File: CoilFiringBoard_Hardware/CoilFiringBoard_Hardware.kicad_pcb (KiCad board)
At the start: 2 copper layers, 101.6 x 76.2 mm, 22 parts, among them Q1 Q_NMOS_GDS, Q2 Q_NMOS_GDS

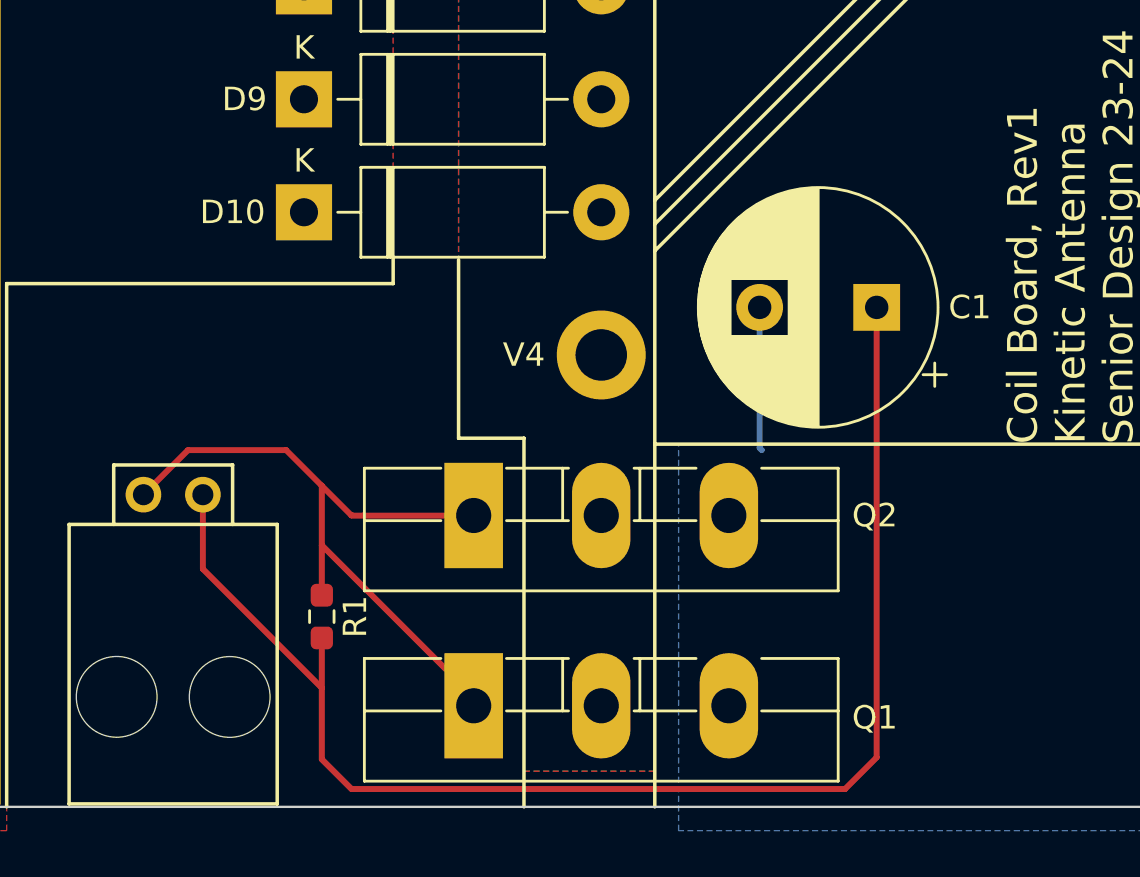
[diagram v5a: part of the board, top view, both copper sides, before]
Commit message: Adjusted gate traces
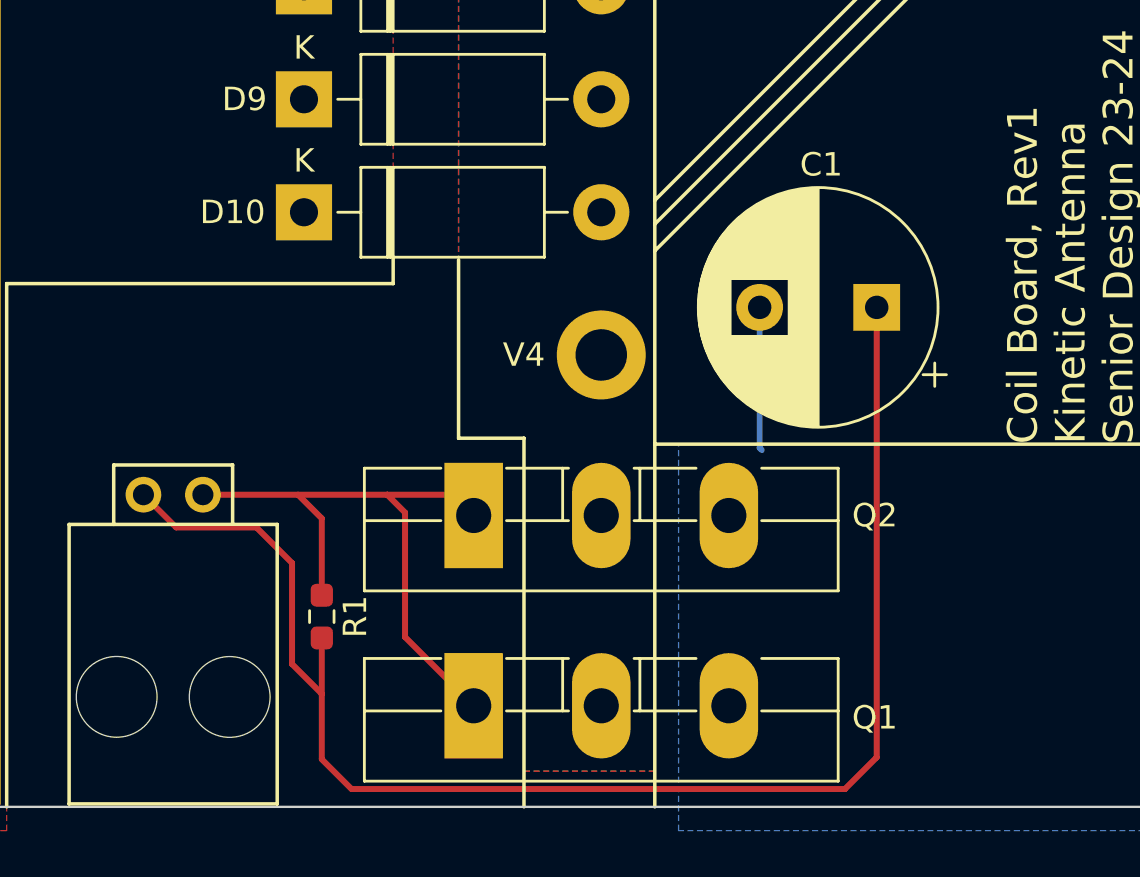
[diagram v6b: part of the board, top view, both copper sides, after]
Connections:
- Conn1 pad 1: GND1 -> Net-(Q1-G)
- Conn1 pad 2: Net-(Q1-G) -> GND1
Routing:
- net GND1: track 59.6 -> 62.9 mm
- net Net-(Q1-G): track 30.3 -> 27.2 mm
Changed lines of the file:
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@@
     (property "ki_keywords" "cap capacitor")
     (attr through_hole)
-    (fp_text reference "C1" (at -3.982323 0) (layer "F.SilkS")
+    (fp_text reference "C1" (at 2.367677 6.096) (layer "F.SilkS")
         (effects (font (size 1 1) (thickness 0.15)))
     )
@@
     (pad "" np_thru_hole circle (at 3.683 -8.636 180) (size 3.45 3.45) (drill 3.45) (layers "*.Cu" "*.Mask"))
     (pad "1" thru_hole circle (at 0 0 180) (size 1.524 1.524) (drill 0.9) (layers "*.Cu" "*.Mask")
+      (net 2 "Net-(Q1-G)") (pintype "input"))
+    (pad "2" thru_hole circle (at 2.54 0 180) (size 1.524 1.524) (drill 0.9) (layers "*.Cu" "*.Mask")
       (net 1 "GND1") (pintype "input"))
-    (pad "2" thru_hole circle (at 2.54 0 180) (size 1.524 1.524) (drill 0.9) (layers "*.Cu" "*.Mask")
-      (net 2 "Net-(Q1-G)") (pintype "input"))
     (model "${MRDT_KICAD_LIBRARIES}/3D Files/MRDT_Connctors/Molex_SL_02_Horizontal.stp"
       (offset (xyz 5.079999924 12.95399981 0))
@@
     (style (thickness 0.15) (arrow_length 1.27) (text_position_mode 0) (extension_height 0.58642) (extension_offset 0.5) keep_text_aligned)
   )
-  (segment (start 97.536 101.473) (end 97.536 104.648) (width 0.254) (layer "F.Cu") (net 1))
-  (segment (start 102.616 109.728) (end 102.616 112.776) (width 0.254) (layer "F.Cu") (net 1))
+  (segment (start 101.346 104.394) (end 99.822 102.87) (width 0.254) (layer "F.Cu") (net 1))
   (segment (start 103.886 114.046) (end 124.968 114.046) (width 0.254) (layer "F.Cu") (net 1))
+  (segment (start 102.616 109.982) (end 101.346 108.712) (width 0.254) (layer "F.Cu") (net 1))
   (segment (start 126.319677 112.694323) (end 126.319677 93.472) (width 0.254) (layer "F.Cu") (net 1))
-  (segment (start 97.536 104.648) (end 102.616 109.728) (width 0.254) (layer "F.Cu") (net 1))
+  (segment (start 102.616 107.5925) (end 102.616 109.982) (width 0.254) (layer "F.Cu") (net 1))
+  (segment (start 102.616 112.776) (end 103.886 114.046) (width 0.254) (layer "F.Cu") (net 1))
+  (segment (start 101.346 108.712) (end 101.346 104.394) (width 0.254) (layer "F.Cu") (net 1))
   (segment (start 124.968 114.046) (end 126.319677 112.694323) (width 0.254) (layer "F.Cu") (net 1))
-  (segment (start 102.616 107.5925) (end 102.616 109.728) (width 0.254) (layer "F.Cu") (net 1))
-  (segment (start 102.616 112.776) (end 103.886 114.046) (width 0.254) (layer "F.Cu") (net 1))
-  (segment (start 109.104 110.49) (end 109.104 110.12) (width 0.254) (layer "F.Cu") (net 2))
-  (segment (start 96.901 99.568) (end 94.996 101.473) (width 0.254) (layer "F.Cu") (net 2))
-  (segment (start 102.616 105.7675) (end 102.616 103.632) (width 0.254) (layer "F.Cu") (net 2))
-  (segment (start 102.616 103.632) (end 102.616 101.092) (width 0.254) (layer "F.Cu") (net 2))
-  (segment (start 101.092 99.568) (end 96.901 99.568) (width 0.254) (layer "F.Cu") (net 2))
-  (segment (start 103.886 102.362) (end 102.616 101.092) (width 0.254) (layer "F.Cu") (net 2))
-  (segment (start 109.104 110.12) (end 102.616 103.632) (width 0.254) (layer "F.Cu") (net 2))
-  (segment (start 102.616 101.092) (end 101.092 99.568) (width 0.254) (layer "F.Cu") (net 2))
-  (segment (start 109.104 102.362) (end 103.886 102.362) (width 0.254) (layer "F.Cu") (net 2))
+  (segment (start 102.616 109.982) (end 102.616 112.776) (width 0.254) (layer "F.Cu") (net 1))
+  (segment (start 96.393 102.87) (end 94.996 101.473) (width 0.254) (layer "F.Cu") (net 1))
+  (segment (start 99.822 102.87) (end 96.393 102.87) (width 0.254) (layer "F.Cu") (net 1))
+  (segment (start 97.536 101.473) (end 101.6 101.473) (width 0.254) (layer "F.Cu") (net 2))
+  (segment (start 102.616 105.7675) (end 102.616 102.489) (width 0.254) (layer "F.Cu") (net 2))
+  (segment (start 106.172 107.558) (end 106.172 102.235) (width 0.254) (layer "F.Cu") (net 2))
+  (segment (start 101.6 101.473) (end 105.41 101.473) (width 0.254) (layer "F.Cu") (net 2))
+  (segment (start 108.215 101.473) (end 109.104 102.362) (width 0.254) (layer "F.Cu") (net 2))
+  (segment (start 106.172 102.235) (end 105.41 101.473) (width 0.254) (layer "F.Cu") (net 2))
+  (segment (start 102.616 102.489) (end 101.6 101.473) (width 0.254) (layer "F.Cu") (net 2))
+  (segment (start 105.41 101.473) (end 108.215 101.473) (width 0.254) (layer "F.Cu") (net 2))
+  (segment (start 109.104 110.49) (end 106.172 107.558) (width 0.254) (layer "F.Cu") (net 2))
   (segment (start 121.319677 99.475677) (end 121.412 99.568) (width 0.254) (layer "B.Cu") (net 4))
   (segment (start 121.319677 93.472) (end 121.319677 99.475677) (width 0.254) (layer "B.Cu") (net 4))

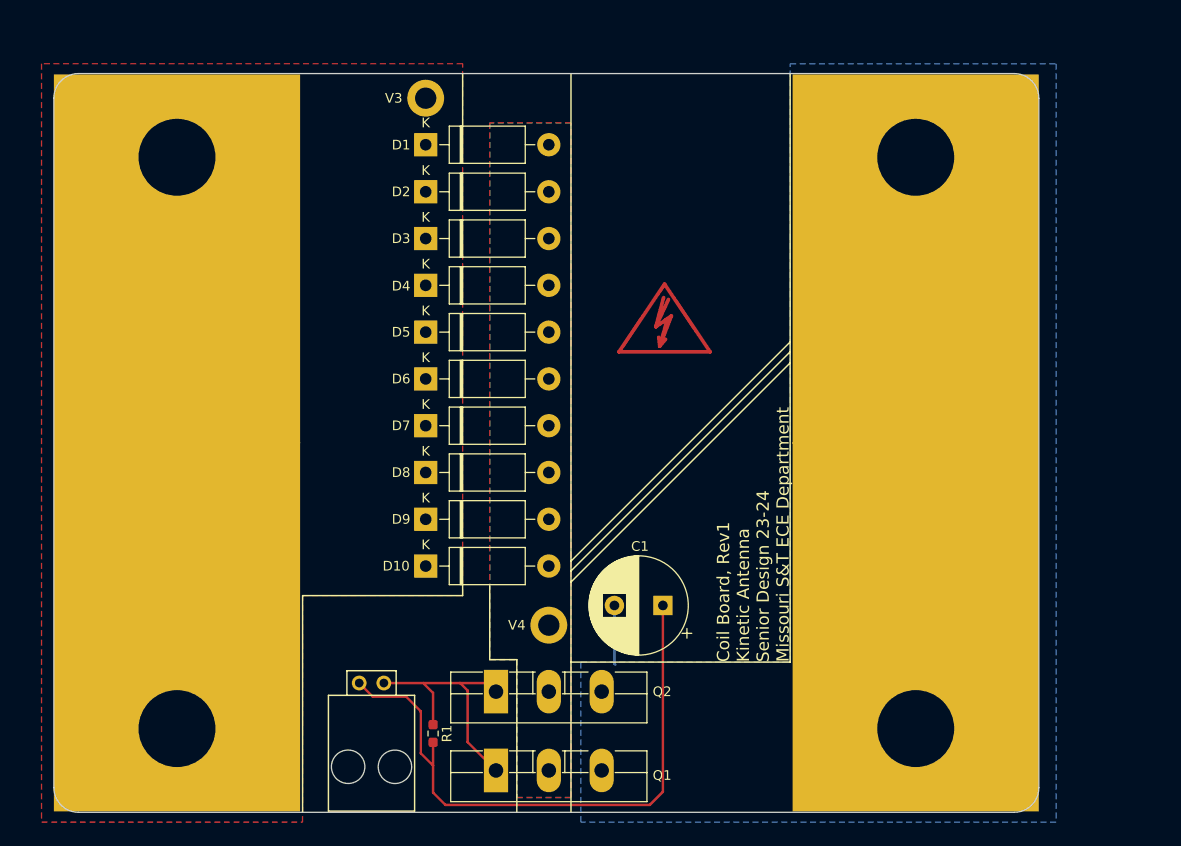
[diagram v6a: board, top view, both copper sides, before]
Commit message: Updated layout
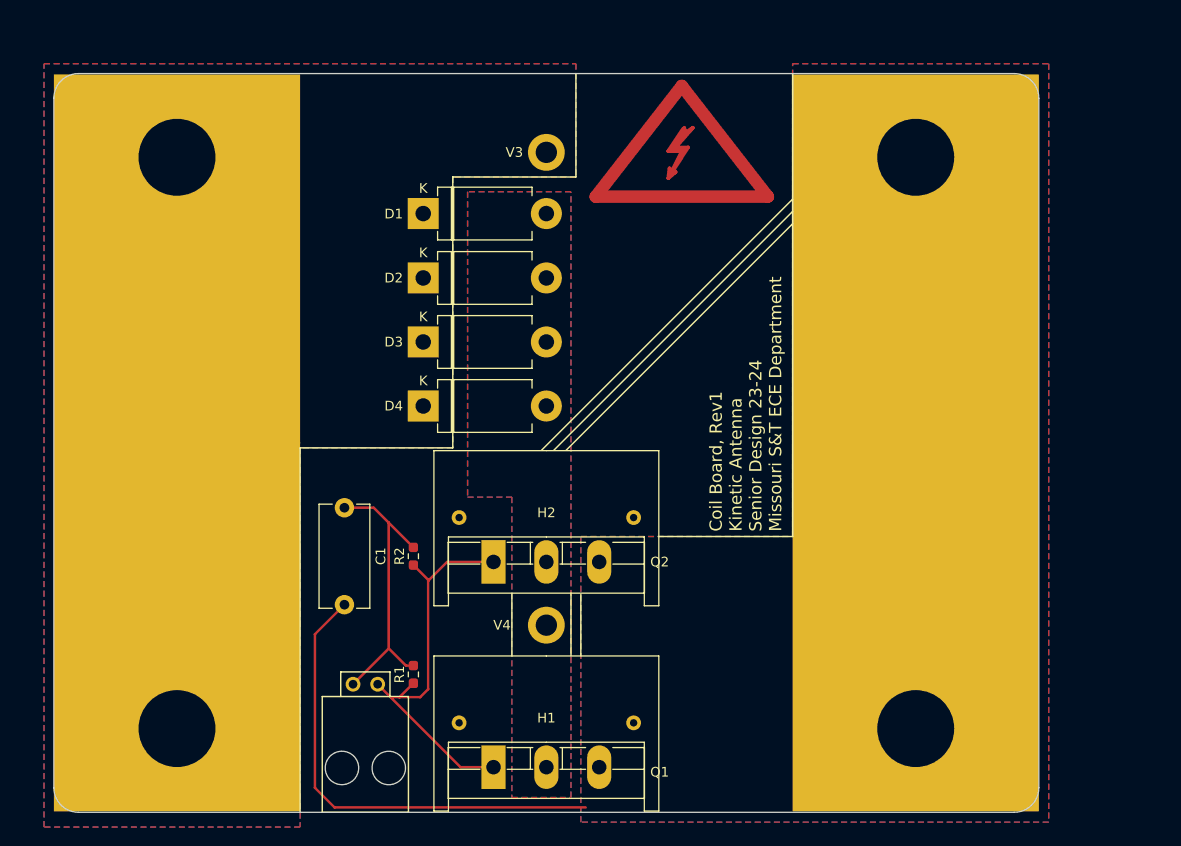
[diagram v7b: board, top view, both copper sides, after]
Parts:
- removed D10, D5, D6, D7, D8, D9: D, Diode_THT:D_DO-15_P12.70mm_Horizontal
- removed the REF** at (126.5, 64.5)
- added H1: ~, SeniorDesign:WV-T264-101E, F.Cu at (114.3, 105.6)
- added H2: ~, SeniorDesign:WV-T264-101E, F.Cu at (114.3, 84.4)
- added R2: 4.7k, Resistor_SMD:R_0603_1608Metric_Pad0.98x0.95mm_HandSolder, F.Cu at (100.6, 88.4)
- added REF**: Symbol_Highvoltage_Type2_CopperTop_Small, Symbol:Symbol_Highvoltage_Type2_CopperTop_Small, F.Cu at (128.3, 47.5)
- C1: footprint Capacitor_THT:CP_Radial_D10.0mm_P5.00mm -> Capacitor_THT:C_Disc_D10.5mm_W5.0mm_P10.00mm
- D1, D2, D3, D4: footprint Diode_THT:D_DO-15_P12.70mm_Horizontal -> Diode_THT:D_DO-201AD_P12.70mm_Horizontal
- moved C1 34.4 mm to (93.5, 83.4), turned to -90 degrees
- moved V3 13.6 mm to (114.3, 46.7)
- moved Q2 13.4 mm to (108.8, 89.0)
- moved D4 12.4 mm to (101.6, 72.9)
- moved D3 10.7 mm to (101.6, 66.3)
- moved D2 8.89 mm to (101.6, 59.7)
- moved D1 7.10 mm to (101.6, 53.0)
- moved R1 6.43 mm to (100.6, 100.6), turned to 90 degrees
- moved Conn1 0.65 mm to (96.9, 101.6)
- moved Q1 0.42 mm to (108.8, 110.2)
- moved V4 0.25 mm to (114.3, 95.5)
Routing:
- net GND: track 6.13 -> 48.9 mm
- net GND1: track 62.9 -> 30.3 mm
- net Net-(Q1-G): track 27.2 -> 42.7 mm
- added copper zone on F.Cu, net GND
- added copper zone on B.Cu, net PWR
